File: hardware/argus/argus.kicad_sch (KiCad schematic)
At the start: 2 parts, among them U1 CH32V003FxPx

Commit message: hardware: Adds connectors for power and data
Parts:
- added J1, J2: Conn_01x02, symbol Connector_Generic:Conn_01x02
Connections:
- net +5V: now also J1.1 (Pin_1)
- net GND: now also J1.2 (Pin_2)
- new net D+: J2.1 (Pin_1)
- new net D-: J2.2 (Pin_2)
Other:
- note added: "HSE CRYSTAL"

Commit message: hardware: Adds 25 MHz HSE crystal
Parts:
- added C2, C3: 20p, symbol Device:C_Small
- added X1: 25MHZ, symbol Device:Crystal
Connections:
- net GND: now also C2.2, C3.2
- net at U1.5 (PA1): now also C2.1, X1.2
- net at U1.6 (PA2): now also C3.1, X1.1

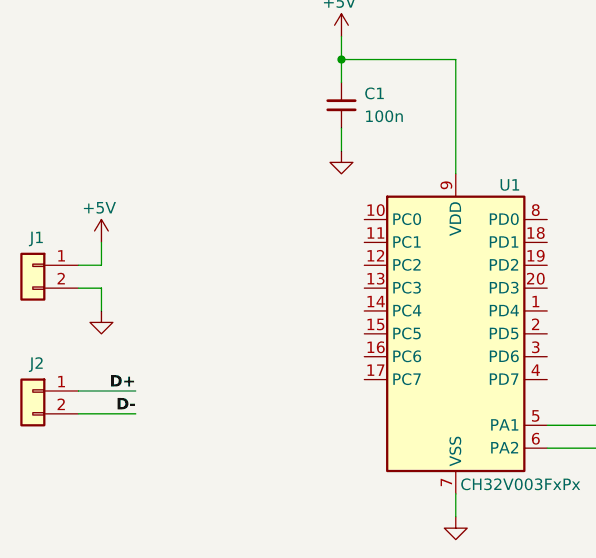
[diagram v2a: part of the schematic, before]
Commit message: hardware: Adds D+ and D- connections
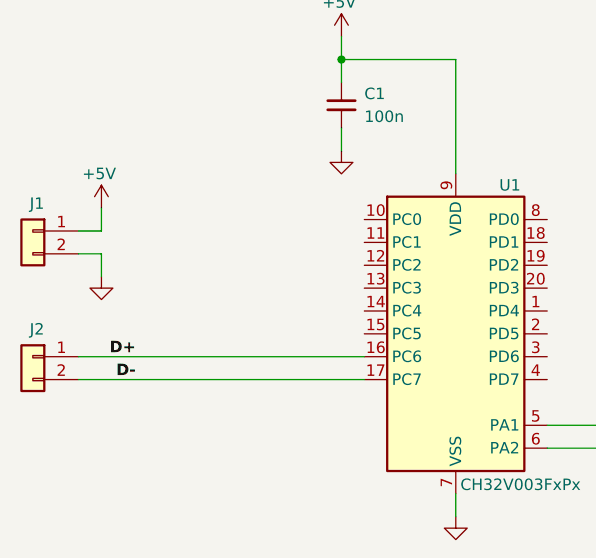
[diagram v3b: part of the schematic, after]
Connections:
- net D+: now also U1.16 (PC6)
- net D-: now also U1.17 (PC7)
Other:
- moved on the sheet: J1, J2
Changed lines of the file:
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@@
 	(wire
 		(pts
-			(xy 97.79 73.66) (xy 100.33 73.66)
+			(xy 97.79 69.85) (xy 100.33 69.85)
 		)
 		(stroke
@@
 	(wire
 		(pts
-			(xy 100.33 76.2) (xy 100.33 78.74)
+			(xy 100.33 72.39) (xy 100.33 74.93)
 		)
 		(stroke
@@
 	(wire
 		(pts
-			(xy 97.79 76.2) (xy 100.33 76.2)
+			(xy 97.79 72.39) (xy 100.33 72.39)
 		)
 		(stroke
@@
 	(wire
 		(pts
-			(xy 100.33 71.12) (xy 100.33 73.66)
-		)
-		(stroke
-			(width 0)
-			(type default)
-		)
-	)
-	(wire
-		(pts
-			(xy 97.79 90.17) (xy 104.14 90.17)
+			(xy 100.33 67.31) (xy 100.33 69.85)
+		)
+		(stroke
+			(width 0)
+			(type default)
+		)
+	)
+	(wire
+		(pts
+			(xy 97.79 86.36) (xy 129.54 86.36)
 		)
 		(stroke
@@
 	(wire
 		(pts
-			(xy 97.79 87.63) (xy 104.14 87.63)
+			(xy 97.79 83.82) (xy 129.54 83.82)
 		)
 		(stroke
@@
 	)
 	(label "D+"
-		(at 104.14 87.63 180)
+		(at 104.14 83.82 180)
 		(effects
 			(font
@@
 	)
 	(label "D-"
-		(at 104.14 90.17 180)
+		(at 104.14 86.36 180)
 		(effects
 			(font
@@
 	(symbol
 		(lib_id "Connector_Generic:Conn_01x02")
-		(at 92.71 73.66 0)
+		(at 92.71 69.85 0)
 		(mirror y)
 		(unit 1)
@@
 		(dnp no)
 		(property "Reference" "J1"
-			(at 93.98 70.612 0)
+			(at 93.98 66.802 0)
 			(show_name no)
 			(do_not_autoplace no)
@@
 		)
 		(property "Value" "Conn_01x02"
-			(at 90.17 76.1999 0)
+			(at 90.17 72.3899 0)
 			(hide yes)
 			(show_name no)
@@
 		)
 		(property "Footprint" ""
-			(at 92.71 73.66 0)
+			(at 92.71 69.85 0)
 			(hide yes)
 			(show_name no)
@@
 		)
 		(property "Datasheet" ""
-			(at 92.71 73.66 0)
+			(at 92.71 69.85 0)
 			(hide yes)
 			(show_name no)
@@
 		)
 		(property "Description" "Generic connector, single row, 01x02, script generated (kicad-library-utils/schlib/autogen/connector/)"
-			(at 92.71 73.66 0)
+			(at 92.71 69.85 0)
 			(hide yes)
 			(show_name no)
@@
 	(symbol
 		(lib_id "Connector_Generic:Conn_01x02")
-		(at 92.71 87.63 0)
+		(at 92.71 83.82 0)
 		(mirror y)
 		(unit 1)
@@
 		(dnp no)
 		(property "Reference" "J2"
-			(at 93.98 84.582 0)
+			(at 93.98 80.772 0)
 			(show_name no)
 			(do_not_autoplace no)
@@
 		)
 		(property "Value" "Conn_01x02"
-			(at 90.17 90.1699 0)
+			(at 90.17 86.3599 0)
 			(hide yes)
 			(show_name no)
@@
 		)
 		(property "Footprint" ""
-			(at 92.71 87.63 0)
+			(at 92.71 83.82 0)
 			(hide yes)
 			(show_name no)
@@
 		)
 		(property "Datasheet" ""
-			(at 92.71 87.63 0)
+			(at 92.71 83.82 0)
 			(hide yes)
 			(show_name no)
@@
 		)
 		(property "Description" "Generic connector, single row, 01x02, script generated (kicad-library-utils/schlib/autogen/connector/)"
-			(at 92.71 87.63 0)
+			(at 92.71 83.82 0)
 			(hide yes)
 			(show_name no)
@@
 	(symbol
 		(lib_id "power:GND")
-		(at 100.33 78.74 0)
+		(at 100.33 74.93 0)
 		(unit 1)
 		(body_style 1)
@@
 		(dnp no)
 		(property "Reference" "#PWR04"
-			(at 100.33 85.09 0)
+			(at 100.33 81.28 0)
 			(hide yes)
 			(show_name no)
@@
 		)
 		(property "Value" "GND"
-			(at 100.33 82.55 0)
+			(at 100.33 78.74 0)
 			(hide yes)
 			(show_name no)
@@
 		)
 		(property "Footprint" ""
-			(at 100.33 78.74 0)
+			(at 100.33 74.93 0)
 			(hide yes)
 			(show_name no)
@@
 		)
 		(property "Datasheet" ""
-			(at 100.33 78.74 0)
+			(at 100.33 74.93 0)
 			(hide yes)
 			(show_name no)
@@
 		)
 		(property "Description" "Power symbol creates a global label with name \"GND\" , ground"
-			(at 100.33 78.74 0)
+			(at 100.33 74.93 0)
 			(hide yes)
 			(show_name no)
@@
 	(symbol
 		(lib_id "power:+5V")
-		(at 100.33 71.12 0)
+		(at 100.33 67.31 0)
 		(unit 1)
 		(body_style 1)
@@
 		(dnp no)
 		(property "Reference" "#PWR05"
-			(at 100.33 74.93 0)
+			(at 100.33 71.12 0)
 			(hide yes)
 			(show_name no)
@@
 		)
 		(property "Value" "+5V"
-			(at 100.076 67.31 0)
+			(at 100.076 63.5 0)
 			(show_name no)
 			(do_not_autoplace no)
@@
 		)
 		(property "Footprint" ""
-			(at 100.33 71.12 0)
+			(at 100.33 67.31 0)
 			(hide yes)
 			(show_name no)
@@
 		)
 		(property "Datasheet" ""
-			(at 100.33 71.12 0)
+			(at 100.33 67.31 0)
 			(hide yes)
 			(show_name no)
@@
 		)
 		(property "Description" "Power symbol creates a global label with name \"+5V\""
-			(at 100.33 71.12 0)
-			(hide yes)
-			(show_name no)
+			(at 100.33 67.31 0)
+			(hide yes)
+			(show_name no)

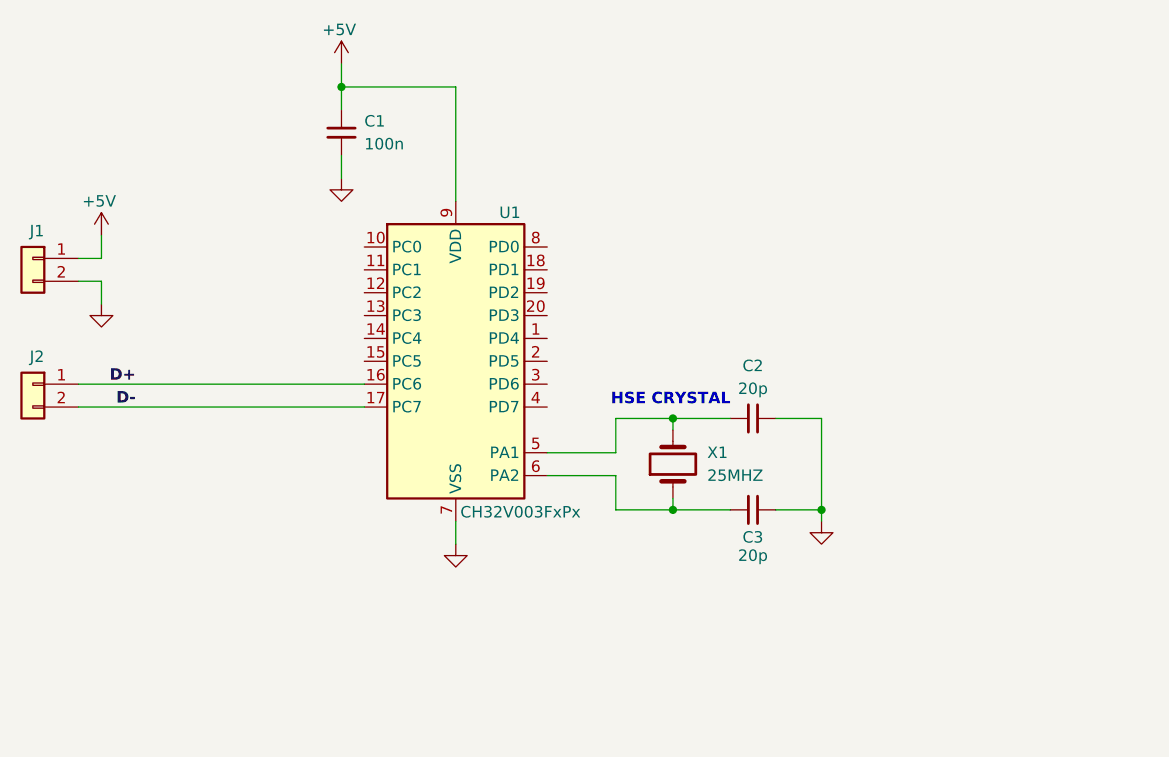
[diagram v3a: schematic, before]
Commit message: hardware: Finishes schematic
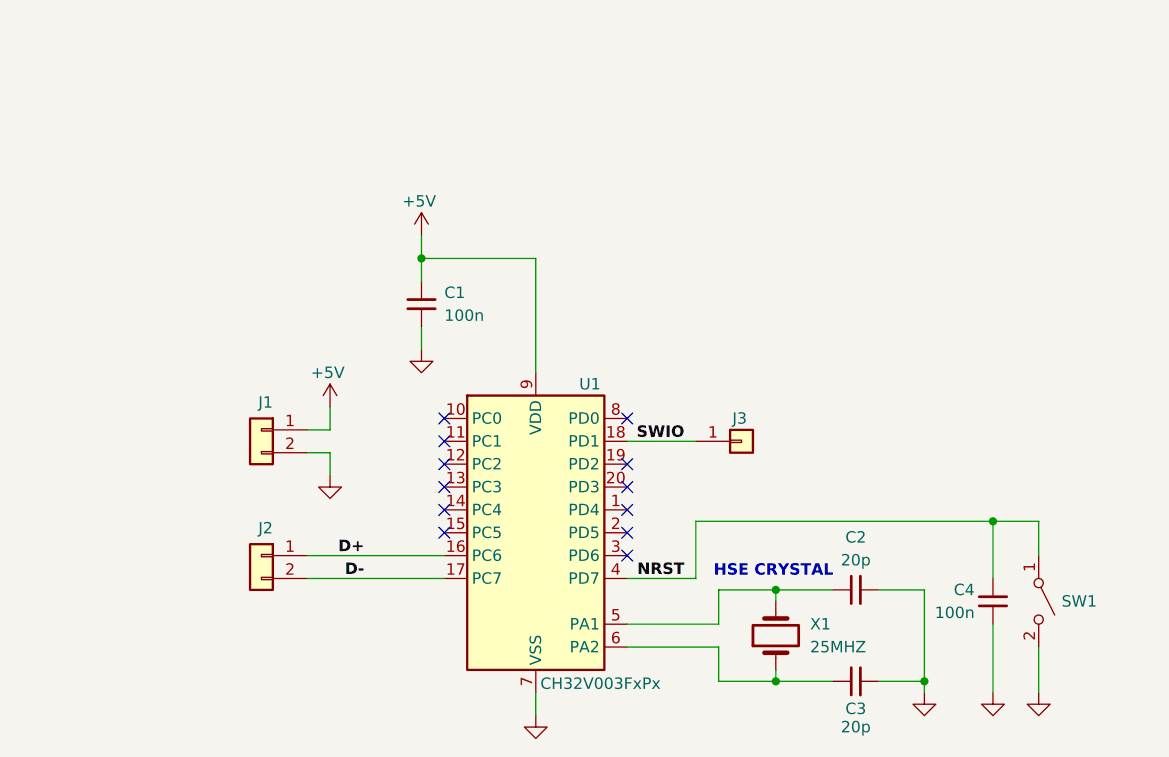
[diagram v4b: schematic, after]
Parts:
- added C4: 100n, symbol Device:C_Small
- added J3: Conn_01x01, symbol Connector_Generic:Conn_01x01
- added SW1: SW_SPST, symbol Switch:SW_SPST
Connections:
- net GND: now also C4.2, SW1.2 (B)
- net SWIO: now reaches U1.18 (PD1)
- net SWIO: now also J3.1 (Pin_1)
- net NRST: now reaches U1.4 (PD7)
- net NRST: now also C4.1, SW1.1 (A)
- no-connect marks 0 -> 12
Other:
- moved on the sheet: C1, C2, C3, J1, J2, U1, X1

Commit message: hardware: Adds PWR flags
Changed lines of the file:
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@@
+	)
+	(junction
+		(at 148.59 69.85)
+		(diameter 0)
+		(color 0 0 0 0)
 	)
 	(junction
@@
 	)
 	(junction
+		(at 148.59 119.38)
+		(diameter 0)
+		(color 0 0 0 0)
+	)
+	(junction
 		(at 175.26 106.68)
 		(diameter 0)
@@
 	(wire
 		(pts
+			(xy 138.43 119.38) (xy 148.59 119.38)
+		)
+		(stroke
+			(width 0)
+			(type default)
+		)
+	)
+	(wire
+		(pts
+			(xy 148.59 67.31) (xy 148.59 69.85)
+		)
+		(stroke
+			(width 0)
+			(type default)
+		)
+	)
+	(wire
+		(pts
 			(xy 199.39 99.06) (xy 199.39 105.41)
 		)
@@
 	(wire
 		(pts
+			(xy 138.43 118.11) (xy 138.43 119.38)
+		)
+		(stroke
+			(width 0)
+			(type default)
+		)
+	)
+	(wire
+		(pts
 			(xy 135.89 67.31) (xy 135.89 69.85)
 		)
@@
 	(wire
 		(pts
+			(xy 148.59 119.38) (xy 148.59 120.65)
+		)
+		(stroke
+			(width 0)
+			(type default)
+		)
+	)
+	(wire
+		(pts
 			(xy 123.19 102.87) (xy 138.43 102.87)
 		)
@@
 	(wire
 		(pts
-			(xy 148.59 118.11) (xy 148.59 120.65)
-		)
-		(stroke
-			(width 0)
-			(type default)
-		)
-	)
-	(wire
-		(pts
 			(xy 186.69 106.68) (xy 191.77 106.68)
 		)
@@
 		(pts
 			(xy 168.91 106.68) (xy 168.91 110.49)
+		)
+		(stroke
+			(width 0)
+			(type default)
+		)
+	)
+	(wire
+		(pts
+			(xy 148.59 118.11) (xy 148.59 119.38)
 		)
 		(stroke
@@
 	)
 	(symbol
+		(lib_id "power:PWR_FLAG")
+		(at 148.59 67.31 0)
+		(unit 1)
+		(body_style 1)
+		(exclude_from_sim no)
+		(in_bom yes)
+		(on_board yes)
+		(in_pos_files yes)
+		(dnp no)
+		(fields_autoplaced yes)
+		(property "Reference" "#FLG01"
+			(at 148.59 65.405 0)
+			(hide yes)
+			(show_name no)
+			(do_not_autoplace no)
+			(effects
+				(font
+					(size 1.27 1.27)
+				)
+			)
+		)
+		(property "Value" "PWR_FLAG"
+			(at 148.59 62.23 0)
+			(hide yes)
+			(show_name no)
+			(do_not_autoplace no)
+			(effects
+				(font
+					(size 1.27 1.27)
+				)
+			)
+		)
+		(property "Footprint" ""
+			(at 148.59 67.31 0)
+			(hide yes)
+			(show_name no)
+			(do_not_autoplace no)
+			(effects
+				(font
+					(size 1.27 1.27)
+				)
+			)
+		)
+		(property "Datasheet" ""
+			(at 148.59 67.31 0)
+			(hide yes)
+			(show_name no)
+			(do_not_autoplace no)
+			(effects
+				(font
+					(size 1.27 1.27)
+				)
+			)
+		)
+		(property "Description" "Special symbol for telling ERC where power comes from"
+			(at 148.59 67.31 0)
+			(hide yes)
+			(show_name no)
+			(do_not_autoplace no)
+			(effects
+				(font
+					(size 1.27 1.27)
+				)
+			)
+		)
+		(pin "1"
+		)
+		(instances
+			(project "argus"
+				(path "/88ede172-e62b-4a6b-80f1-e187fed87fb7"
+					(reference "#FLG01")
+					(unit 1)
+				)
+			)
+		)
+	)
+	(symbol
 		(lib_id "power:GND")
 		(at 125.73 93.98 0)
@@
 					(unit 1)
 				)
+			)
+		)
+	)
+	(symbol
+		(lib_id "power:PWR_FLAG")
+		(at 138.43 118.11 0)
+		(unit 1)
+		(body_style 1)
+		(exclude_from_sim no)
+		(in_bom yes)
+		(on_board yes)
+		(in_pos_files yes)
+		(dnp no)
+		(fields_autoplaced yes)
+		(property "Reference" "#FLG02"
+			(at 138.43 116.205 0)
+			(hide yes)
+			(show_name no)
+			(do_not_autoplace no)
+			(effects
+				(font
+					(size 1.27 1.27)
+				)
+			)
+		)
+		(property "Value" "PWR_FLAG"
+			(at 138.43 113.03 0)
+			(hide yes)
+			(show_name no)
+			(do_not_autoplace no)
+			(effects
+				(font
+					(size 1.27 1.27)
+				)
+			)
+		)
+		(property "Footprint" ""
+			(at 138.43 118.11 0)
+			(hide yes)
+			(show_name no)
+			(do_not_autoplace no)
+			(effects
+				(font
+					(size 1.27 1.27)
+				)
+			)
+		)
+		(property "Datasheet" ""
+			(at 138.43 118.11 0)
+			(hide yes)
+			(show_name no)
+			(do_not_autoplace no)
+			(effects
+				(font
+					(size 1.27 1.27)
+				)
+			)
+		)
+		(property "Description" "Special symbol for telling ERC where power comes from"
+			(at 138.43 118.11 0)
+			(hide yes)
+			(show_name no)
+			(do_not_autoplace no)
+			(effects
+				(font
+					(size 1.27 1.27)
+				)
+			)
+		)
+		(pin "1"
+		)
+		(instances
+			(project "argus"
+				(path "/88ede172-e62b-4a6b-80f1-e187fed87fb7"
+					(reference "#FLG02")
+					(unit 1)
+				)

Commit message: hardware: Assigns footprints
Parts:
- C1, C2, C3, C4: footprint (none) -> Capacitor_SMD:C_0603_1608Metric
- J1, J2: footprint (none) -> Connector_Wire:SolderWire-0.5sqmm_1x02_P4.6mm_D0.9mm_OD2.1mm
- J3: footprint (none) -> Connector_Pin:Pin_D1.0mm_L10.0mm
- SW1: footprint (none) -> Button_Switch_SMD:SW_DIP_SPSTx01_Slide_6.7x4.1mm_W6.73mm_P2.54mm_LowProfile_JPin
- X1: value 25MHZ -> 24MHZ; footprint (none) -> Crystal:Crystal_SMD_Abracon_ABM8G-4Pin_3.2x2.5mm
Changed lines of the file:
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@@
 			)
 		)
-		(property "Footprint" ""
+		(property "Footprint" "Capacitor_SMD:C_0603_1608Metric"
 			(at 184.15 106.68 0)
 			(hide yes)
@@
 			)
 		)
-		(property "Footprint" ""
+		(property "Footprint" "Connector_Wire:SolderWire-0.5sqmm_1x02_P4.6mm_D0.9mm_OD2.1mm"
 			(at 118.11 88.9 0)
 			(hide yes)
@@
 			)
 		)
-		(property "Footprint" ""
+		(property "Footprint" "Capacitor_SMD:C_0603_1608Metric"
 			(at 199.39 107.95 0)
 			(hide yes)
@@
 			)
 		)
-		(property "Footprint" ""
+		(property "Footprint" "Connector_Wire:SolderWire-0.5sqmm_1x02_P4.6mm_D0.9mm_OD2.1mm"
 			(at 118.11 102.87 0)
 			(hide yes)
@@
 			)
 		)
-		(property "Footprint" ""
+		(property "Footprint" "Capacitor_SMD:C_0603_1608Metric"
 			(at 135.89 74.93 0)
 			(hide yes)
@@
 			)
 		)
-		(property "Footprint" ""
+		(property "Footprint" "Capacitor_SMD:C_0603_1608Metric"
 			(at 184.15 116.84 0)
 			(hide yes)
@@
 			)
 		)
-		(property "Footprint" ""
+		(property "Footprint" "Connector_Pin:Pin_D1.0mm_L10.0mm"
 			(at 171.45 90.17 0)
 			(hide yes)
@@
 			)
 		)
-		(property "Footprint" ""
+		(property "Footprint" "Button_Switch_SMD:SW_DIP_SPSTx01_Slide_6.7x4.1mm_W6.73mm_P2.54mm_LowProfile_JPin"
 			(at 204.47 107.95 0)
 			(hide yes)
@@
 			)
 		)
-		(property "Value" "25MHZ"
+		(property "Value" "24MHZ"
 			(at 179.07 113.0299 90)
 			(show_name no)
@@
 			)
 		)
-		(property "Footprint" ""
+		(property "Footprint" "Crystal:Crystal_SMD_Abracon_ABM8G-4Pin_3.2x2.5mm"
 			(at 175.26 111.76 0)
 			(hide yes)
@@
 			)
 		)
-		(property "Datasheet" ""
+		(property "Datasheet" "https://eu.mouser.com/en/ProductDetail/ABRACON/ASE2-24.000MHZ-L-C-T?qs=s46Hw6dZPL7XHJx%252Bx4DWOw%3D%3D"
 			(at 175.26 111.76 0)
 			(hide yes)

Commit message: hardware: First layout proposition
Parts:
- removed J1, J2: Conn_01x02, Connector_Wire:SolderWire-0.5sqmm_1x02_P4.6mm_D0.9mm_OD2.1mm, symbol Connector_Generic:Conn_01x02
- added J1, J2, J3, J4: Conn_01x01, Connector_Pin:Pin_D0.7mm_L6.5mm_W1.8mm_FlatFork, symbol Connector_Generic:Conn_01x01
- J5: renamed from J3; footprint Connector_Pin:Pin_D1.0mm_L10.0mm -> Connector_Pin:Pin_D0.7mm_L6.5mm_W1.8mm_FlatFork
- SW1: footprint Button_Switch_SMD:SW_DIP_SPSTx01_Slide_6.7x4.1mm_W6.73mm_P2.54mm_LowProfile_JPin -> Button_Switch_SMD:SW_SPST_EVQPE1
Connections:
- net +5V: now also J1.1 (Pin_1)
- net D+: now also J3.1 (Pin_1)
- net D-: now also J4.1 (Pin_1)
- net GND: now also J2.1 (Pin_1)

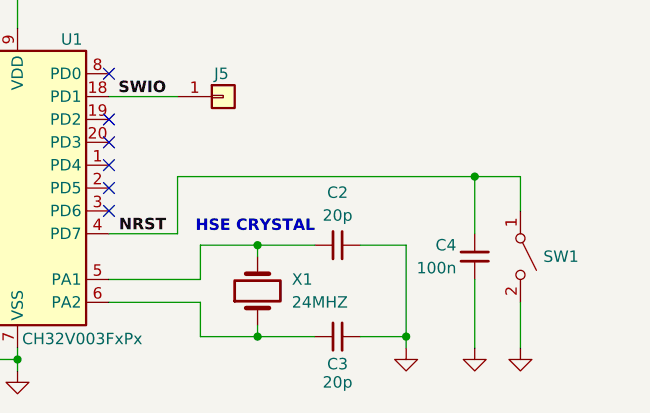
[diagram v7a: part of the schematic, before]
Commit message: hardware: Changes XTAL footprint. Adjusts layout
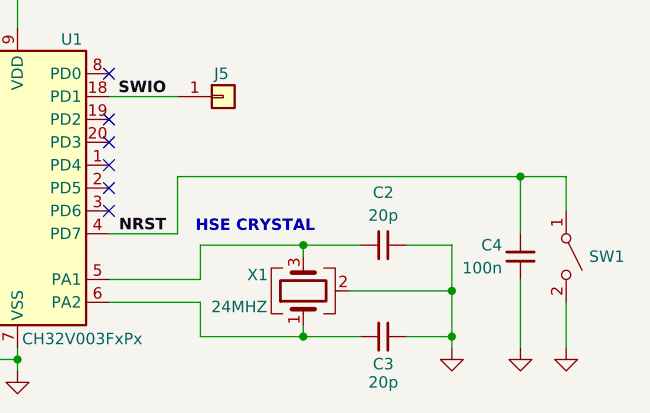
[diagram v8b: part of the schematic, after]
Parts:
- removed X1: 24MHZ, Crystal:Crystal_SMD_Abracon_ABM8G-4Pin_3.2x2.5mm, symbol Device:Crystal
- added X1: 24MHZ, Crystal:Crystal_SMD_2520-4Pin_2.5x2.0mm, symbol Device:Crystal_GND24
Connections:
- net GND: now also X1.2 (G), X1.4 (G)
- net at C2.1, U1.5 (PA1): now also X1.3
- net at C3.1, U1.6 (PA2): now also X1.1
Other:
- moved on the sheet: C2, C3, C4, SW1
